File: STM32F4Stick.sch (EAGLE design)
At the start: 42 parts, among them U1 MIC5219 3.3V, U2 USD-SOCKETNEW

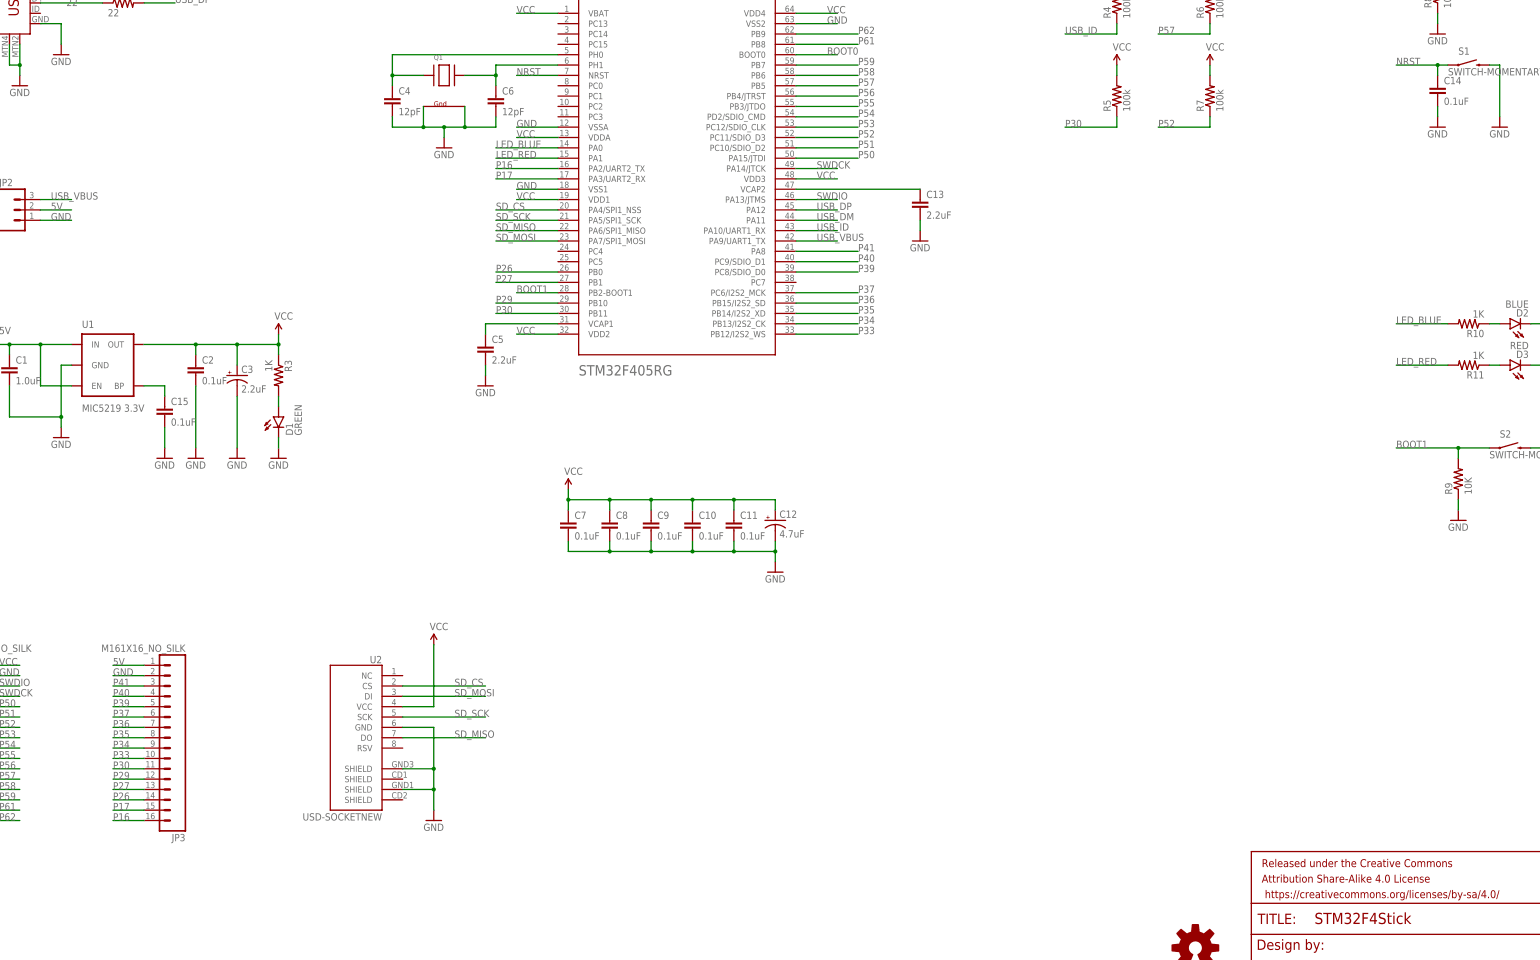
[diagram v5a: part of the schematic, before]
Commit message: Final Rev B. Added nRF24L01+ 2.4GHz radio compatible header. Got rid of some of the extension headers. Check out RevA if you do not need to use nRF24L01+ radio but instead have extension headers.
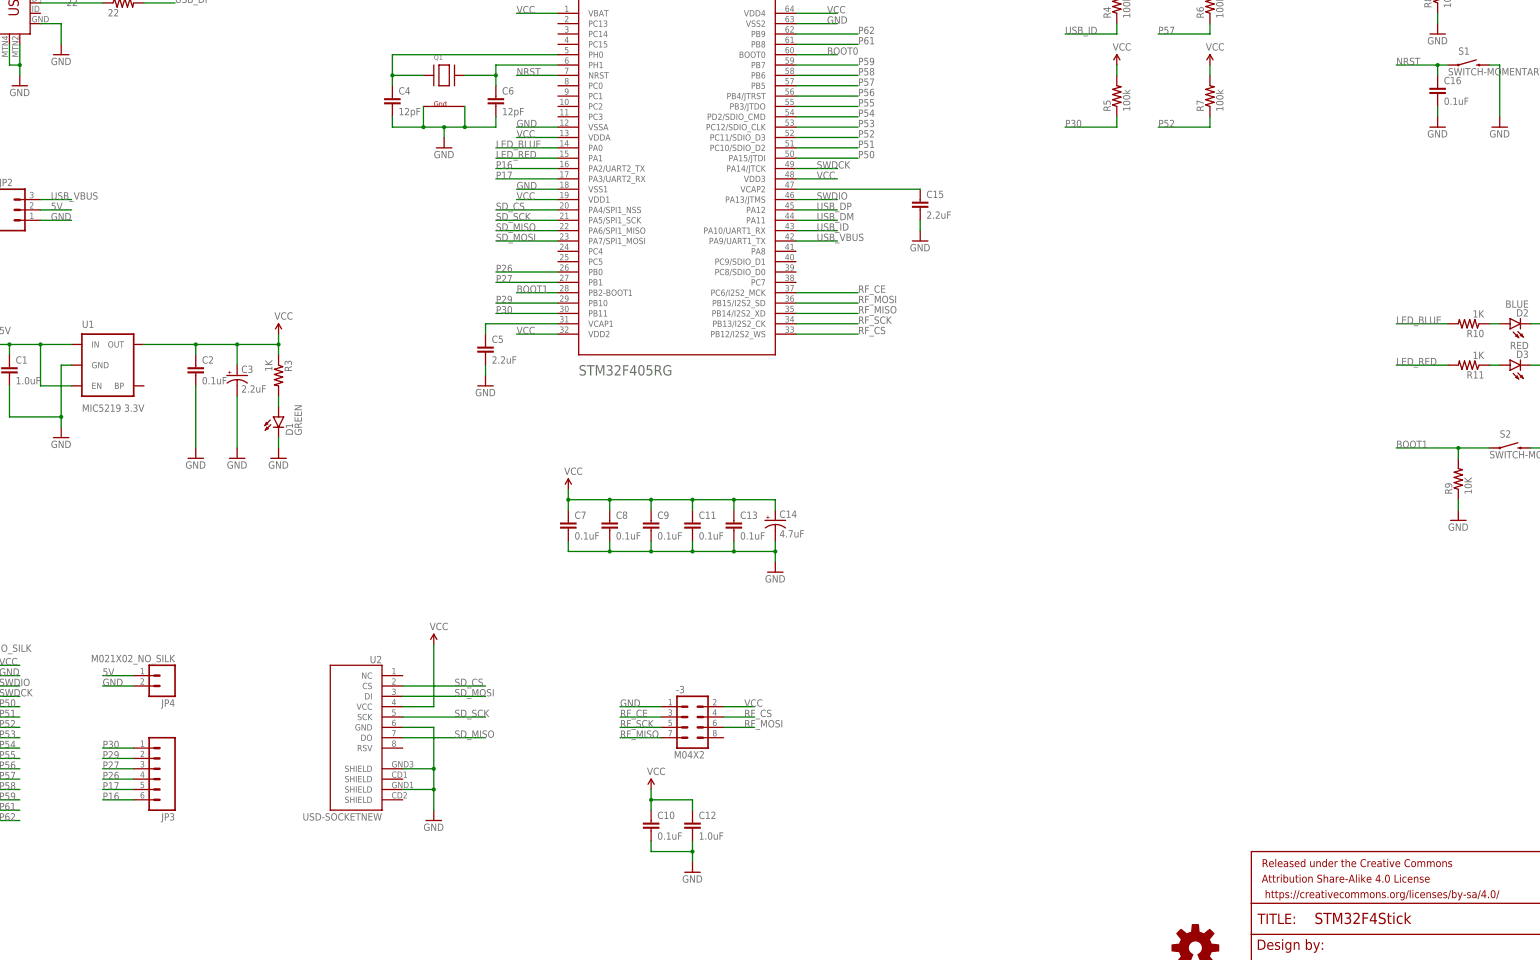
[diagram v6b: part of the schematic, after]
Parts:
- added -3: M04X2, SparkFun-Connectors:M04X2
- added C16: 0.1uF, SparkFun-Capacitors:0.1UF-25V-5%(0603)
- added JP4: M021X02_NO_SILK, SparkFun-Connectors:M021X02_NO_SILK
- C12: value 4.7uF -> 1.0uF; device SparkFun-Capacitors:CAP_POL1206 -> SparkFun-Capacitors:1.0UF-16V-10%(0603)
- C13: value 2.2uF -> 0.1uF; device SparkFun-Capacitors:2.2UF-10V-20%(0603) -> SparkFun-Capacitors:0.1UF-25V-5%(0603)
- C14: value 0.1uF -> 4.7uF; device SparkFun-Capacitors:0.1UF-25V-5%(0603) -> SparkFun-Capacitors:CAP_POL1206
- C15: value 0.1uF -> 2.2uF; device SparkFun-Capacitors:0.1UF-25V-5%(0603) -> SparkFun-Capacitors:2.2UF-10V-20%(0603)
- JP3: value M161X16_NO_SILK -> (none); device SparkFun-Connectors:M161X16_NO_SILK -> SparkFun-Connectors:M06NO_SILK
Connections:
- removed net N$2: C15.1, U1.BP
- removed net P33: -2.PB12/I2S2_WS, JP3.10
- removed net P34: -2.PB13/I2S2_CK, JP3.9
- removed net P35: -2.PB14/I2S2_XD, JP3.8
- removed net P36: -2.PB15/I2S2_SD, JP3.7
- removed net P37: -2.PC6/I2S2_MCK, JP3.6
- removed net P39: -2.PC8/SDIO_D0, JP3.5
- removed net P40: -2.PC9/SDIO_D1, JP3.4
- removed net P41: -2.PA8, JP3.3
- new net RF_CE: -2.PC6/I2S2_MCK, -3.3
- new net RF_CS: -2.PB12/I2S2_WS, -3.4
- new net RF_MISO: -2.PB14/I2S2_XD, -3.7
- new net RF_MOSI: -2.PB15/I2S2_SD, -3.6
- new net RF_SCK: -2.PB13/I2S2_CK, -3.5
- net 5V: now also JP4.1; no longer JP3.1
- net GND: now also -3.1, C12.2, C14.-, C16.2, JP4.2; no longer C12.-, C14.2, JP3.2
- net N$10: now also C15.1; no longer C13.1
- net NRST: now also C16.1; no longer C14.1
- net P16: now also JP3.6; no longer JP3.16
- net P17: now also JP3.5; no longer JP3.15
- net P26: now also JP3.4; no longer JP3.14
- net P27: now also JP3.3; no longer JP3.13
- net P29: now also JP3.2; no longer JP3.12
- net P30: now also JP3.1; no longer JP3.11
- net VCC: now also -3.2, C12.1, C13.1, C14.+; no longer C12.+
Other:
- note added: "B"
- note added: "nrf24l01+ 2.4GHz radio connector Added two decoupling capacitors"
- note removed: "A"
- moved on the sheet: C10, C11, C13, C15

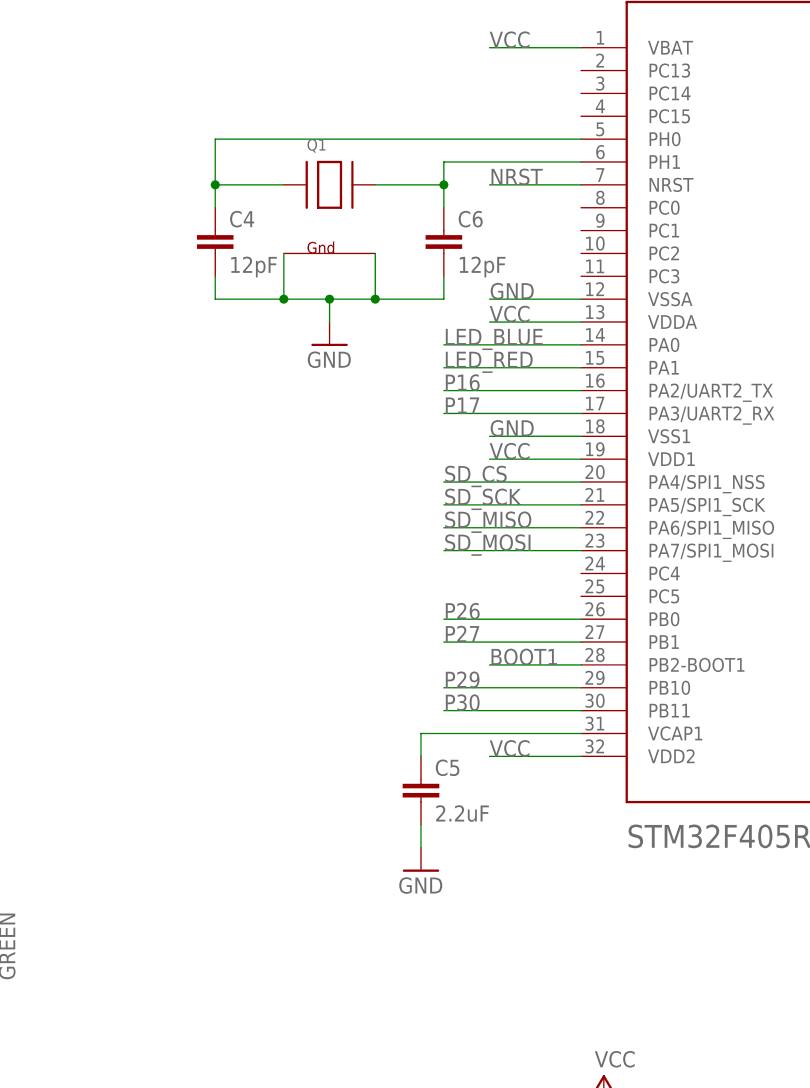
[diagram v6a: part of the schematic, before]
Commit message: adeed STM32F401 chip support to schematic only
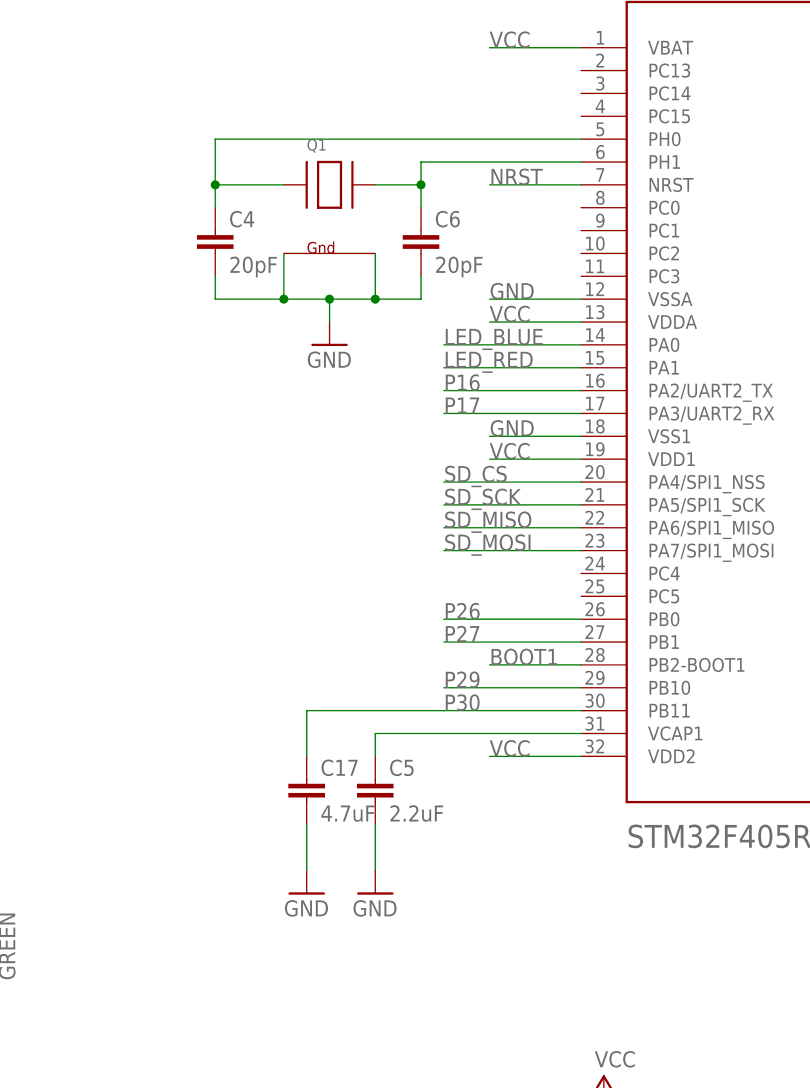
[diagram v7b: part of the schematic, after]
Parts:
- added C17: 4.7uF, SparkFun-Capacitors:4.7UF-6.3V-10%(0603)0603
- C4, C6: value 12pF -> 20pF
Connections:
- net GND: now also C17.2
- net P30: now also C17.1
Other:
- note added: "C"
- note added: "Decoupling capacitors for the STM32F4 chip Place one cap per VDD pin"
- note added: "For STM32F401 compatibility, C15 should be 0 ohm resistor"
- note added: "For STM32F401 compatibility, C5 should be 0 ohm resistor For STM32F405, don't fit C17"
- note removed: "B"
- note removed: "Decoupling capacitors for the STM32F405 chip Place one cap per VDD pin"
- moved on the sheet: C5, C6
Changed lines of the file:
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@@
 <part name="SUPPLY3" library="SparkFun-Aesthetics" deviceset="VCC" device=""/>
 <part name="GND9" library="SparkFun-Aesthetics" deviceset="GND" device=""/>
-<part name="C6" library="SparkFun-Capacitors" deviceset="12PF-50V-5%(0603)" device="" value="12pF"/>
-<part name="C4" library="SparkFun-Capacitors" deviceset="12PF-50V-5%(0603)" device="" value="12pF"/>
+<part name="C6" library="SparkFun-Capacitors" deviceset="12PF-50V-5%(0603)" device="" value="20pF"/>
+<part name="C4" library="SparkFun-Capacitors" deviceset="12PF-50V-5%(0603)" device="" value="20pF"/>
 <part name="C3" library="SparkFun-Capacitors" deviceset="CAP_POL" device="1206" value="2.2uF"/>
 <part name="GND6" library="SparkFun-Aesthetics" deviceset="GND" device=""/>
@@
 <part name="SUPPLY4" library="SparkFun-Aesthetics" deviceset="VCC" device=""/>
 <part name="GND11" library="SparkFun-Aesthetics" deviceset="GND" device=""/>
+<part name="GND19" library="SparkFun-Aesthetics" deviceset="GND" device=""/>
+<part name="C17" library="SparkFun-Capacitors" deviceset="4.7UF-6.3V-10%(0603)" device="0603" value="4.7uF"/>
 </parts>
 <sheets>
@@
 <plain>
 <text x="170.18" y="127" size="1.778" layer="150">Decoupling capacitors
-for the STM32F405 chip
+for the STM32F4 chip
 Place one cap per VDD pin</text>
 <text x="365.76" y="264.16" size="1.778" layer="150">Short SJ1 to put the chip into
@@
 <text x="10.16" y="88.9" size="1.778" layer="150">Extra connection headers</text>
 <text x="355.6" y="7.62" size="5.08" layer="150">Furkan Cayci</text>
-<text x="426.72" y="7.62" size="5.08" layer="150">B</text>
+<text x="426.72" y="7.62" size="5.08" layer="150">C</text>
 <text x="22.86" y="261.62" size="1.778" layer="150">USB can be used for programming through bootloader
 It requires an external oscillator to be hooked up</text>
@@
 <text x="175.26" y="86.36" size="1.778" layer="150">nrf24l01+ 2.4GHz radio connector
 Added two decoupling capacitors</text>
+<wire x1="124.46" y1="170.18" x2="142.24" y2="170.18" width="0.2032" layer="150"/>
+<wire x1="142.24" y1="170.18" x2="142.24" y2="142.24" width="0.2032" layer="150"/>
+<wire x1="142.24" y1="142.24" x2="124.46" y2="142.24" width="0.2032" layer="150"/>
+<wire x1="124.46" y1="170.18" x2="124.46" y2="142.24" width="0.2032" layer="150"/>
+<text x="99.06" y="172.72" size="1.778" layer="150">For STM32F401 compatibility,
+C5 should be 0 ohm resistor
+For STM32F405, don't fit C17</text>
+<text x="243.84" y="200.66" size="1.778" layer="150">For STM32F401 compatibility,
+C15 should be 0 ohm resistor</text>
 </plain>
 <instances>
 <instance part="-2" gate="G$1" x="187.96" y="200.66"/>
-<instance part="C5" gate="G$1" x="142.24" y="157.48"/>
+<instance part="C5" gate="G$1" x="137.16" y="157.48"/>
 <instance part="C15" gate="G$1" x="248.92" y="193.04"/>
 <instance part="GND13" gate="1" x="248.92" y="185.42"/>
@@
 <instance part="R8" gate="G$1" x="375.92" y="246.38" rot="R90"/>
 <instance part="GND14" gate="1" x="375.92" y="236.22"/>
-<instance part="GND10" gate="1" x="142.24" y="149.86"/>
+<instance part="GND10" gate="1" x="137.16" y="147.32"/>
 <instance part="SUPPLY9" gate="G$1" x="391.16" y="256.54"/>
 <instance part="JP1" gate="G$1" x="10.16" y="60.96" rot="MR180"/>
@@
 <instance part="SUPPLY3" gate="G$1" x="162.56" y="124.46"/>
 <instance part="GND9" gate="1" x="132.08" y="208.28"/>
-<instance part="C6" gate="G$1" x="144.78" y="218.44"/>
+<instance part="C6" gate="G$1" x="142.24" y="218.44"/>
 <instance part="C4" gate="G$1" x="119.38" y="218.44"/>
 <instance part="C3" gate="G$1" x="81.28" y="152.4"/>
@@
 <instance part="SUPPLY4" gate="G$1" x="182.88" y="50.8"/>
 <instance part="GND11" gate="1" x="193.04" y="30.48"/>
+<instance part="GND19" gate="1" x="129.54" y="147.32"/>
+<instance part="C17" gate="G$1" x="129.54" y="157.48"/>
 </instances>
 <busses>
@@
 <pinref part="C5" gate="G$1" pin="2"/>
 <pinref part="GND10" gate="1" pin="GND"/>
-<wire x1="142.24" y1="152.4" x2="142.24" y2="154.94" width="0.1524" layer="91"/>
+<wire x1="137.16" y1="149.86" x2="137.16" y2="154.94" width="0.1524" layer="91"/>
 </segment>
 <segment>
@@
 <pinref part="C6" gate="G$1" pin="2"/>
 <wire x1="127" y1="213.36" x2="132.08" y2="213.36" width="0.1524" layer="91"/>
-<wire x1="144.78" y1="215.9" x2="144.78" y2="213.36" width="0.1524" layer="91"/>
-<wire x1="144.78" y1="213.36" x2="137.16" y2="213.36" width="0.1524" layer="91"/>
+<wire x1="142.24" y1="215.9" x2="142.24" y2="213.36" width="0.1524" layer="91"/>
+<wire x1="142.24" y1="213.36" x2="137.16" y2="213.36" width="0.1524" layer="91"/>
 <junction x="132.08" y="213.36"/>
 <pinref part="Q1" gate="G$1" pin="G2"/>
@@
 <junction x="193.04" y="35.56"/>
 </segment>
+<segment>
+<pinref part="GND19" gate="1" pin="GND"/>
+<pinref part="C17" gate="G$1" pin="2"/>
+<wire x1="129.54" y1="154.94" x2="129.54" y2="149.86" width="0.1524" layer="91"/>
+</segment>
 </net>
 <net name="N$10" class="0">
@@
 <segment>
 <pinref part="-2" gate="G$1" pin="PH1"/>
-<wire x1="160.02" y1="228.6" x2="144.78" y2="228.6" width="0.1524" layer="91"/>
-<wire x1="144.78" y1="228.6" x2="144.78" y2="226.06" width="0.1524" layer="91"/>
+<wire x1="160.02" y1="228.6" x2="142.24" y2="228.6" width="0.1524" layer="91"/>
+<wire x1="142.24" y1="228.6" x2="142.24" y2="226.06" width="0.1524" layer="91"/>
 <pinref part="C6" gate="G$1" pin="1"/>
 <pinref part="Q1" gate="G$1" pin="X2"/>
-<wire x1="137.16" y1="226.06" x2="144.78" y2="226.06" width="0.1524" layer="91"/>
-<wire x1="144.78" y1="226.06" x2="144.78" y2="223.52" width="0.1524" layer="91"/>
-<junction x="144.78" y="226.06"/>
+<wire x1="137.16" y1="226.06" x2="142.24" y2="226.06" width="0.1524" layer="91"/>
+<wire x1="142.24" y1="226.06" x2="142.24" y2="223.52" width="0.1524" layer="91"/>
+<junction x="142.24" y="226.06"/>
 </segment>
 </net>
@@
 <segment>
 <pinref part="-2" gate="G$1" pin="VCAP1"/>
-<wire x1="160.02" y1="165.1" x2="142.24" y2="165.1" width="0.1524" layer="91"/>
-<wire x1="142.24" y1="165.1" x2="142.24" y2="162.56" width="0.1524" layer="91"/>
+<wire x1="160.02" y1="165.1" x2="137.16" y2="165.1" width="0.1524" layer="91"/>
+<wire x1="137.16" y1="165.1" x2="137.16" y2="162.56" width="0.1524" layer="91"/>
 <pinref part="C5" gate="G$1" pin="1"/>
 </segment>
@@
 <wire x1="160.02" y1="167.64" x2="144.78" y2="167.64" width="0.1524" layer="91"/>
 <label x="144.78" y="167.64" size="1.778" layer="95"/>
-</segment>
-<segment>
+<wire x1="144.78" y1="167.64" x2="129.54" y2="167.64" width="0.1524" layer="91"/>
+<wire x1="129.54" y1="167.64" x2="129.54" y2="162.56" width="0.1524" layer="91"/>
+<pinref part="C17" gate="G$1" pin="1"/>
+</segment>
+<segment>

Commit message: V2 RevB final. Finalize stm32f401 support on version 2 board.
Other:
- note added: "B"
- note added: "Version 2"
- note removed: "C"
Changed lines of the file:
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@@
 <text x="10.16" y="88.9" size="1.778" layer="150">Extra connection headers</text>
 <text x="355.6" y="7.62" size="5.08" layer="150">Furkan Cayci</text>
-<text x="426.72" y="7.62" size="5.08" layer="150">C</text>
+<text x="426.72" y="7.62" size="5.08" layer="150">B</text>
 <text x="22.86" y="261.62" size="1.778" layer="150">USB can be used for programming through bootloader
 It requires an external oscillator to be hooked up</text>
@@
 <text x="243.84" y="200.66" size="1.778" layer="150">For STM32F401 compatibility,
 C15 should be 0 ohm resistor</text>
+<text x="398.78" y="17.78" size="3.81" layer="150">Version 2</text>
 </plain>
 <instances>
